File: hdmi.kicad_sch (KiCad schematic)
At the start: 0 parts

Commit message: Finished the schematic capture for thel HDMI
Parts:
- added C17, C18, C19, C20, C21, C22, C23, C24: 100NF/50V, A_HDJ_Library:C_0402_1005Metric, symbol Device:C_Small
- added C89: 100nF/50V, symbol Device:C_Small
- added D1, D2, D3: ESD5V0B03, A_HDJ_Library:D_0402_1005Metric, symbol Diode:ESD9B5.0ST5G
- added D4: 1N5819WS, A_HDJ_Library:D_SOD-323, symbol Diode:1N5819WS
- added F1: 6V/50MA, A_HDJ_Library:C_0603_1608Metric, symbol Device:Fuse
- added J3: HDMI_A, A_HDJ_Library:HDMI_A_Molex_208658-1001_Horizontal, symbol Connector:HDMI_A
- added Q1: 2N7002, A_HDJ_Library:SOT-23, symbol Transistor_FET:2N7002
- added Q3 (x2), Q4: 2SK3018, A_HDJ_Library:SOT-23, symbol Transistor_FET:2N7002
- added R10, R11, R12, R13, R14, R15, R16, R7, R8, R9: 470R/1%, A_HDJ_Library:R_0402_1005Metric, symbol Device:R
- added R11: 1M/1%, A_HDJ_Library:R_0402_1005Metric, symbol Device:R
- added R15, R18: 2.2k/1%, A_HDJ_Library:R_0402_1005Metric, symbol Device:R
- added R19: 2.2K/1%, A_HDJ_Library:R_0402_1005Metric, symbol Device:R
- added R4: 1M, A_HDJ_Library:R_0402_1005Metric, symbol Device:R
- added R6: 1K/1%, A_HDJ_Library:R_0402_1005Metric, symbol Device:R
- added U1, U2: D3V3XA4B10LP, A_HDJ_Library:Diodes_UDFN-10_1.0x2.5mm_P0.5mm, symbol Power_Protection:D3V3XA4B10LP
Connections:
- new net: F1.2, J3.18 (+5V)
- new net: Q4.1 (G), R19.1
- new net: Q4.3 (D), R10.2, R11.2, R12.2, R13.2, R14.2, R7.2, R8.2, R9.2
- new net: Q1.2 (S), R11.1, R6.1
- new net +3.3V: Q1.1 (G), Q3.1 (G), R15.1, R16.1, R4.1
- new net +5V: D4.2 (A)
- new net 5V_HDMI_VCC: C89.1, D4.1 (K), F1.1, R15.1, R18.1
- new net DDC_SCA: D3.2 (A2), J3.16 (SDA), Q3.2 (S), R18.2
- new net DDC_SCL: D1.2 (A2), J3.15 (SCL), Q3.2 (S), R15.2
- new net DDI_B_HPD: Q1.3 (D), R4.2
- new net DDI_B_TX0+: C17.1, C19.1, C21.1, C23.1
- new net DDI_B_TX0-: C18.1, C20.1, C22.1, C24.1
- new net DDI_DDC_SCA: Q3.3 (D), R15.2
- new net DDI_DDC_SCL: Q3.3 (D), R16.2
- new net GND: C89.2, D1.1 (A1), D2.1 (A1), D3.1 (A1), J3.11 (CKS), J3.17 (GND), J3.2 (D2S), J3.5 (D1S), J3.8 (D0S), J3.SH, Q4.2 (S), R6.2, U1.3 (VSS), U1.8 (VSS), U2.3 (VSS), U2.8 (VSS)
- new net HPD: D2.2 (A2), J3.19 (HPD), R11.2
- new net TMDS_CK+: C23.2, J3.10 (CK+), R8.1, U2.4, U2.7 (NC)
- new net TMDS_CK-: C24.2, J3.12 (CK-), R7.1, U2.5, U2.6 (NC)
- new net TMDS_D0+: C21.2, J3.7 (D0+), R10.1, U2.1, U2.10 (NC)
- new net TMDS_D0-: C22.2, J3.9 (D0-), R9.1, U2.2, U2.9 (NC)
- new net TMDS_D1+: C19.2, J3.4 (D1+), R12.1, U1.4, U1.7 (NC)
- new net TMDS_D1-: C20.2, J3.6 (D1-), R11.1, U1.5, U1.6 (NC)
- new net TMDS_D2+: C17.2, J3.1 (D2+), R14.1, U1.1, U1.10 (NC)
- new net TMDS_D2-: C18.2, J3.3 (D2-), R13.1, U1.2, U1.9 (NC)
- new net ~{PWR_LED}/~{PSON}: R19.2
- no-connect marks 0 -> 1

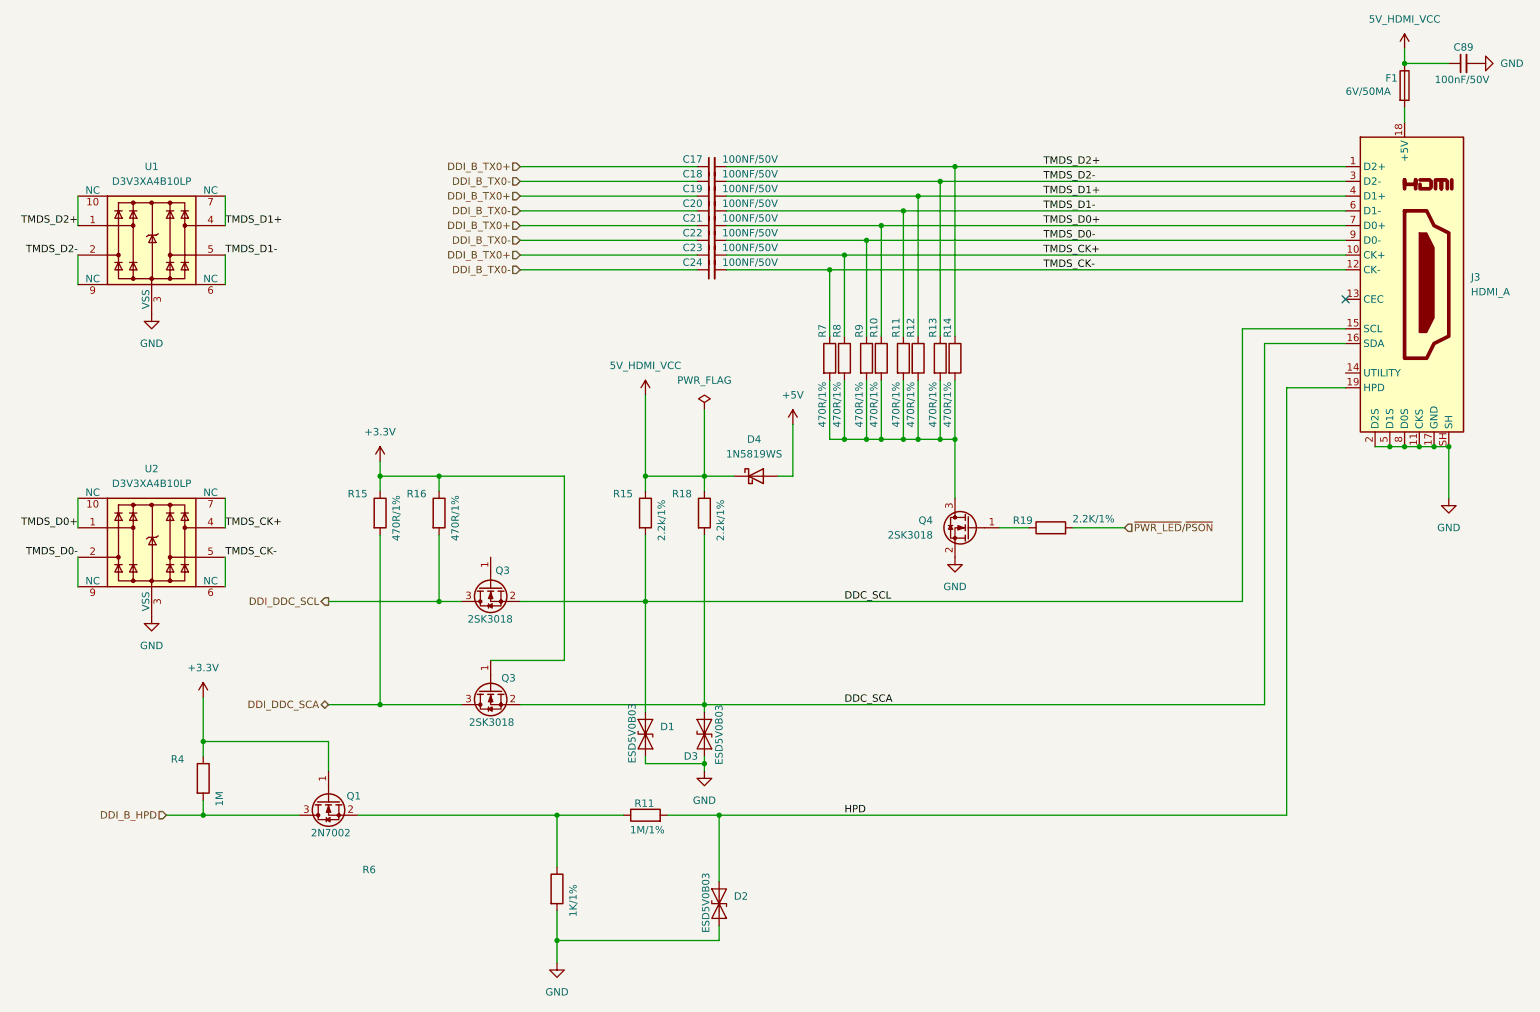
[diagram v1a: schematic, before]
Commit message: Finished the HDMI circuit and connected labels to Mu model in root sheet
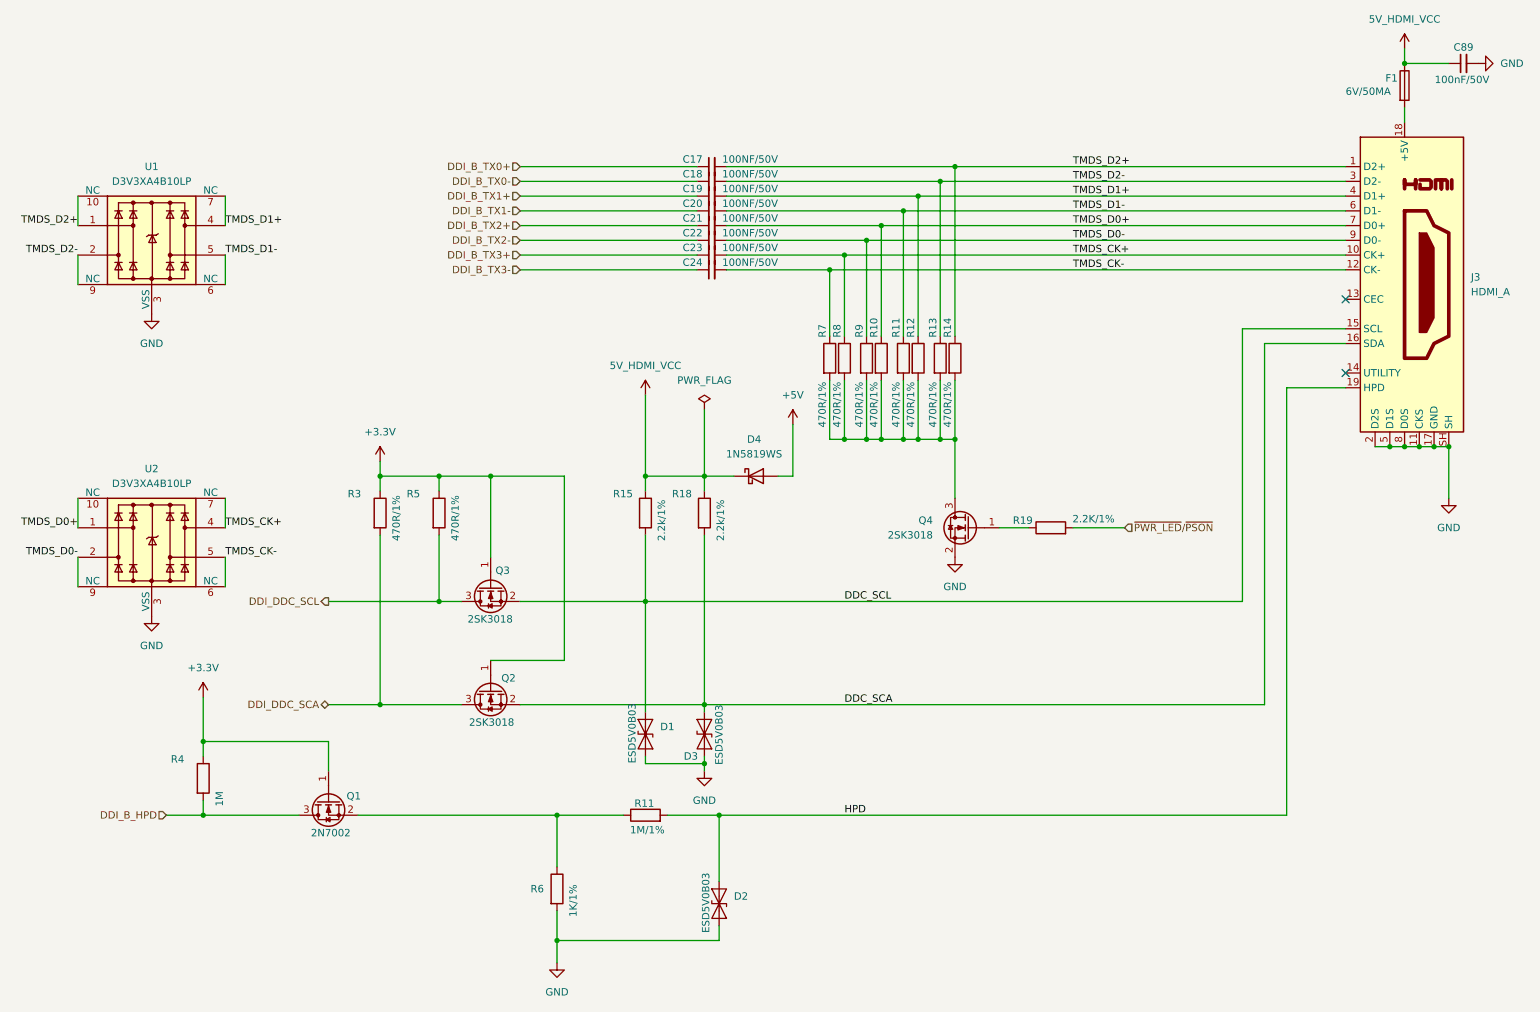
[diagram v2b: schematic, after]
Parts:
- renumbered Q3 to Q2, R15 to R3, R16 to R5
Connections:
- net +3.3V: now also Q3.1 (G)
- net DDI_B_TX0+: no longer C19.1, C21.1, C23.1
- net DDI_B_TX0-: no longer C20.1, C22.1, C24.1
- new net DDI_B_TX1+: C19.1
- new net DDI_B_TX1-: C20.1
- new net DDI_B_TX2+: C21.1
- new net DDI_B_TX2-: C22.1
- new net DDI_B_TX3+: C23.1
- new net DDI_B_TX3-: C24.1
- no-connect marks 1 -> 2
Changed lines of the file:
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@@
 	)
 	(junction
+		(at 106.68 93.98)
+		(diameter 0)
+		(color 0 0 0 0)
+	)
+	(junction
 		(at 264.16 88.9)
 		(diameter 0)
@@
 		(at 254 63.5)
 	)
+	(no_connect
+		(at 254 76.2)
+	)
 	(wire
 		(pts
@@
 	(wire
 		(pts
+			(xy 264.16 30.48) (xy 264.16 33.02)
+		)
+		(stroke
+			(width 0)
+			(type default)
+		)
+	)
+	(wire
+		(pts
 			(xy 111.76 50.8) (xy 142.24 50.8)
 		)
@@
 	(wire
 		(pts
-			(xy 119.38 93.98) (xy 97.79 93.98)
+			(xy 119.38 93.98) (xy 106.68 93.98)
 		)
 		(stroke
@@
 	(wire
 		(pts
-			(xy 264.16 30.48) (xy 264.16 33.02)
-		)
-		(stroke
-			(width 0)
-			(type default)
-		)
-	)
-	(wire
-		(pts
 			(xy 146.05 171.45) (xy 146.05 173.99)
 		)
@@
 	(wire
 		(pts
+			(xy 106.68 93.98) (xy 97.79 93.98)
+		)
+		(stroke
+			(width 0)
+			(type default)
+		)
+	)
+	(wire
+		(pts
 			(xy 35.56 55.88) (xy 35.56 60.96)
 		)
@@
 	(wire
 		(pts
+			(xy 106.68 93.98) (xy 106.68 107.95)
+		)
+		(stroke
+			(width 0)
+			(type default)
+		)
+	)
+	(wire
+		(pts
 			(xy 60.96 97.79) (xy 60.96 102.87)
 		)
@@
 		)
 	)
-	(label "TMDS_CK+"
-		(at 201.93 55.88 0)
+	(label "TMDS_D2-"
+		(at 207.01 43.18 0)
 		(effects
 			(font
@@
 		)
 	)
-	(label "TMDS_D2+"
-		(at 201.93 40.64 0)
+	(label "TMDS_D1+"
+		(at 207.01 45.72 0)
 		(effects
 			(font
@@
 		)
 	)
-	(label "TMDS_D1-"
-		(at 201.93 48.26 0)
+	(label "TMDS_D0-"
+		(at 207.01 53.34 0)
 		(effects
 			(font
@@
 		)
 	)
-	(label "TMDS_D2-"
-		(at 201.93 43.18 0)
+	(label "TMDS_CK+"
+		(at 60.96 102.87 0)
 		(effects
 			(font
@@
 		)
 	)
-	(label "TMDS_CK+"
-		(at 60.96 102.87 0)
+	(label "TMDS_CK-"
+		(at 60.96 107.95 0)
 		(effects
 			(font
@@
 		)
 	)
-	(label "TMDS_CK-"
-		(at 60.96 107.95 0)
+	(label "TMDS_CK+"
+		(at 207.01 55.88 0)
 		(effects
 			(font
@@
 		)
 	)
-	(label "TMDS_D0-"
-		(at 201.93 53.34 0)
+	(label "TMDS_D0+"
+		(at 35.56 102.87 180)
 		(effects
 			(font
 				(size 1.27 1.27)
 			)
-			(justify left bottom)
+			(justify right bottom)
 		)
 	)
-	(label "TMDS_D1+"
-		(at 201.93 45.72 0)
+	(label "TMDS_CK-"
+		(at 207.01 58.42 0)
 		(effects
 			(font
@@
 		)
 	)
-	(label "TMDS_CK-"
-		(at 201.93 58.42 0)
+	(label "TMDS_D1-"
+		(at 207.01 48.26 0)
 		(effects
 			(font
@@
 		)
 	)
-	(label "TMDS_D0+"
-		(at 35.56 102.87 180)
+	(label "TMDS_D2-"
+		(at 35.56 55.88 180)
 		(effects
 			(font
@@
 		)
 	)
-	(label "TMDS_D0+"
-		(at 201.93 50.8 0)
+	(label "TMDS_D2+"
+		(at 207.01 40.64 0)
 		(effects
 			(font
@@
 		)
 	)
-	(label "TMDS_D2-"
-		(at 35.56 55.88 180)
+	(label "TMDS_D0+"
+		(at 207.01 50.8 0)
 		(effects
 			(font
 				(size 1.27 1.27)
 			)
-			(justify right bottom)
+			(justify left bottom)
 		)
 	)
-	(hierarchical_label "DDI_DDC_SCL"
-		(shape output)
-		(at 78.74 115.57 180)
+	(hierarchical_label "DDI_B_TX2+"
+		(shape input)
+		(at 111.76 50.8 180)
 		(effects
 			(font
@@
 		)
 	)
-	(hierarchical_label "DDI_B_TX0+"
+	(hierarchical_label "DDI_B_TX3-"
 		(shape input)
-		(at 111.76 40.64 180)
+		(at 111.76 58.42 180)
 		(effects
 			(font
@@
 		)
 	)
-	(hierarchical_label "DDI_B_TX0+"
+	(hierarchical_label "DDI_B_TX2-"
 		(shape input)
-		(at 111.76 55.88 180)
+		(at 111.76 53.34 180)
 		(effects
 			(font
@@
 		)
 	)
-	(hierarchical_label "DDI_B_TX0+"
-		(shape input)
-		(at 111.76 45.72 180)
+	(hierarchical_label "DDI_DDC_SCA"
+		(shape bidirectional)
+		(at 78.74 133.35 180)
 		(effects
 			(font
@@
 		)
 	)
-	(hierarchical_label "DDI_B_TX0-"
+	(hierarchical_label "DDI_B_TX1+"
 		(shape input)
-		(at 111.76 48.26 180)
+		(at 111.76 45.72 180)
 		(effects
 			(font
@@
 		)
 	)
-	(hierarchical_label "DDI_B_TX0-"
-		(shape input)
-		(at 111.76 53.34 180)
+	(hierarchical_label "DDI_DDC_SCL"
+		(shape output)
+		(at 78.74 115.57 180)
 		(effects
 			(font
@@
 		)
 	)
-	(hierarchical_label "DDI_B_HPD"
+	(hierarchical_label "DDI_B_TX0+"
 		(shape input)
-		(at 50.8 152.4 180)
+		(at 111.76 40.64 180)
 		(effects
 			(font
@@
 		)
 	)
-	(hierarchical_label "DDI_B_TX0-"
+	(hierarchical_label "DDI_B_HPD"
 		(shape input)
-		(at 111.76 58.42 180)
+		(at 50.8 152.4 180)
 		(effects
 			(font
@@
 		)
 	)
-	(hierarchical_label "DDI_DDC_SCA"
-		(shape bidirectional)
-		(at 78.74 133.35 180)
+	(hierarchical_label "DDI_B_TX3+"
+		(shape input)
+		(at 111.76 55.88 180)
 		(effects
 			(font
@@
 		)
 	)
-	(hierarchical_label "DDI_B_TX0+"
+	(hierarchical_label "DDI_B_TX1-"
 		(shape input)
-		(at 111.76 50.8 180)
+		(at 111.76 48.26 180)
 		(effects
 			(font
@@
 		(in_pos_files yes)
 		(dnp no)
-		(property "Reference" "R16"
+		(property "Reference" "R5"
 			(at 92.202 97.028 0)
 			(show_name no)
@@
 			(project "Carrier_Board"
 				(path "/e768274e-12f3-4f83-96f6-abb7638e0bc1/1c6e1139-d819-4324-bacb-4e7c941be195"
-					(reference "R16")
+					(reference "R5")
 					(unit 1)
 				)
@@
 		(dnp no)
 		(property "Reference" "R6"
-			(at 84.582 161.798 0)
+			(at 113.538 165.1 0)
 			(show_name no)
 			(do_not_autoplace no)
@@
 		(in_pos_files yes)
 		(dnp no)
-		(property "Reference" "R15"
+		(property "Reference" "R3"
 			(at 82.042 97.028 0)
 			(show_name no)
@@
 			(project "Carrier_Board"
 				(path "/e768274e-12f3-4f83-96f6-abb7638e0bc1/1c6e1139-d819-4324-bacb-4e7c941be195"
-					(reference "R15")
+					(reference "R3")
 					(unit 1)
 				)
@@
 		(in_pos_files yes)
 		(dnp no)
-		(property "Reference" "Q3"
+		(property "Reference" "Q2"
 			(at 110.998 128.778 90)
 			(show_name no)
@@
 			(project "Carrier_Board"
 				(path "/e768274e-12f3-4f83-96f6-abb7638e0bc1/1c6e1139-d819-4324-bacb-4e7c941be195"
-					(reference "Q3")
+					(reference "Q2")
 					(unit 1)
 				)

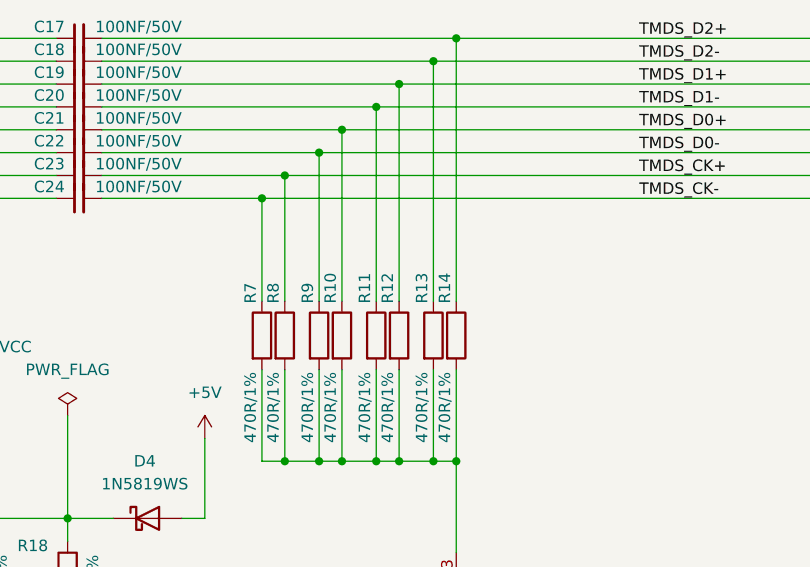
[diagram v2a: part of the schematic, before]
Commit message: Fixed annotation errors duplicate designators on passive components R11 and J15 so that schematic could be imported into pcb. There might be some missing footprints... starting that investigation
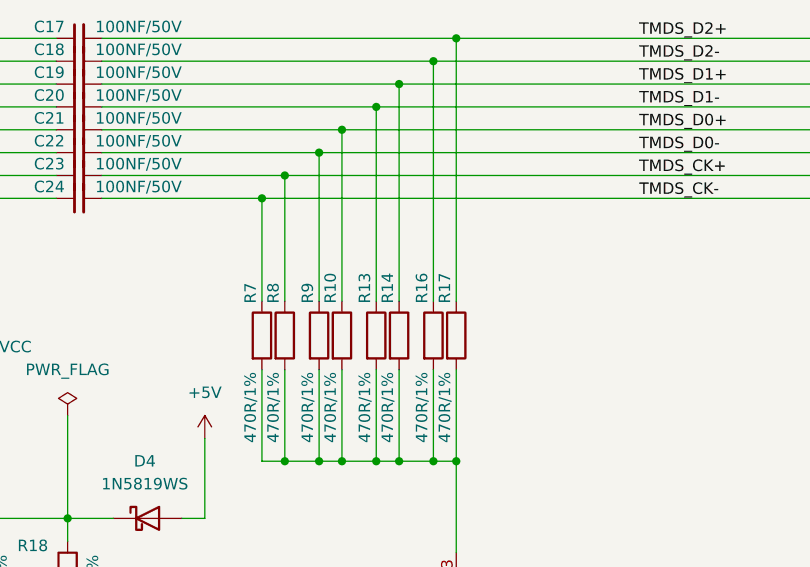
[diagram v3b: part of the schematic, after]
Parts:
- renumbered R11 to R13, R12 to R14, R13 to R16, R14 to R17
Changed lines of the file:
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@@
 		(in_pos_files yes)
 		(dnp no)
-		(property "Reference" "R14"
+		(property "Reference" "R17"
 			(at 185.42 70.104 90)
 			(show_name no)
@@
 			(project "Carrier_Board"
 				(path "/e768274e-12f3-4f83-96f6-abb7638e0bc1/1c6e1139-d819-4324-bacb-4e7c941be195"
-					(reference "R14")
+					(reference "R17")
 					(unit 1)
 				)
@@
 		(in_pos_files yes)
 		(dnp no)
-		(property "Reference" "R13"
+		(property "Reference" "R16"
 			(at 182.88 70.104 90)
 			(show_name no)
@@
 			(project "Carrier_Board"
 				(path "/e768274e-12f3-4f83-96f6-abb7638e0bc1/1c6e1139-d819-4324-bacb-4e7c941be195"
-					(reference "R13")
+					(reference "R16")
 					(unit 1)
 				)
@@
 		(in_pos_files yes)
 		(dnp no)
-		(property "Reference" "R12"
+		(property "Reference" "R14"
 			(at 179.07 70.104 90)
 			(show_name no)
@@
 			(project "Carrier_Board"
 				(path "/e768274e-12f3-4f83-96f6-abb7638e0bc1/1c6e1139-d819-4324-bacb-4e7c941be195"
-					(reference "R12")
+					(reference "R14")
 					(unit 1)
 				)
@@
 		(in_pos_files yes)
 		(dnp no)
-		(property "Reference" "R11"
+		(property "Reference" "R13"
 			(at 176.53 70.104 90)
 			(show_name no)
@@
 			(project "Carrier_Board"
 				(path "/e768274e-12f3-4f83-96f6-abb7638e0bc1/1c6e1139-d819-4324-bacb-4e7c941be195"
-					(reference "R11")
-					(unit 1)
-				)
+					(reference "R13")
+					(unit 1)
+				)
